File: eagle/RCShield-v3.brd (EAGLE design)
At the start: 92.7 x 82.5 mm, 52 parts, among them J1/J2 JOYSTICKPTH, P1/P3 POT, P2/P4 POT, Q1 MMBT3906, U1 TOUSCRUINO_SHIELD, U2 FT232RL-BASICSSOP, U4 XBEE, X1 USBSMD

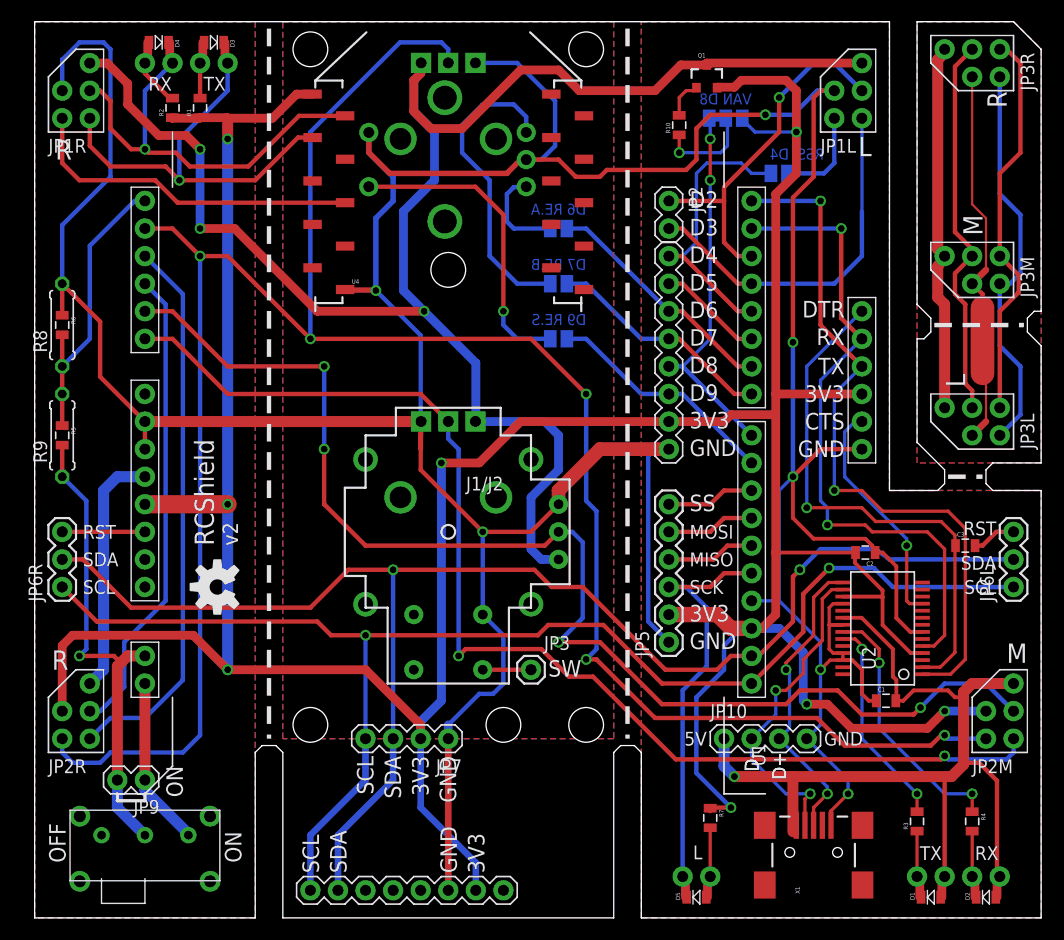
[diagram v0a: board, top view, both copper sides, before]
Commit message: 
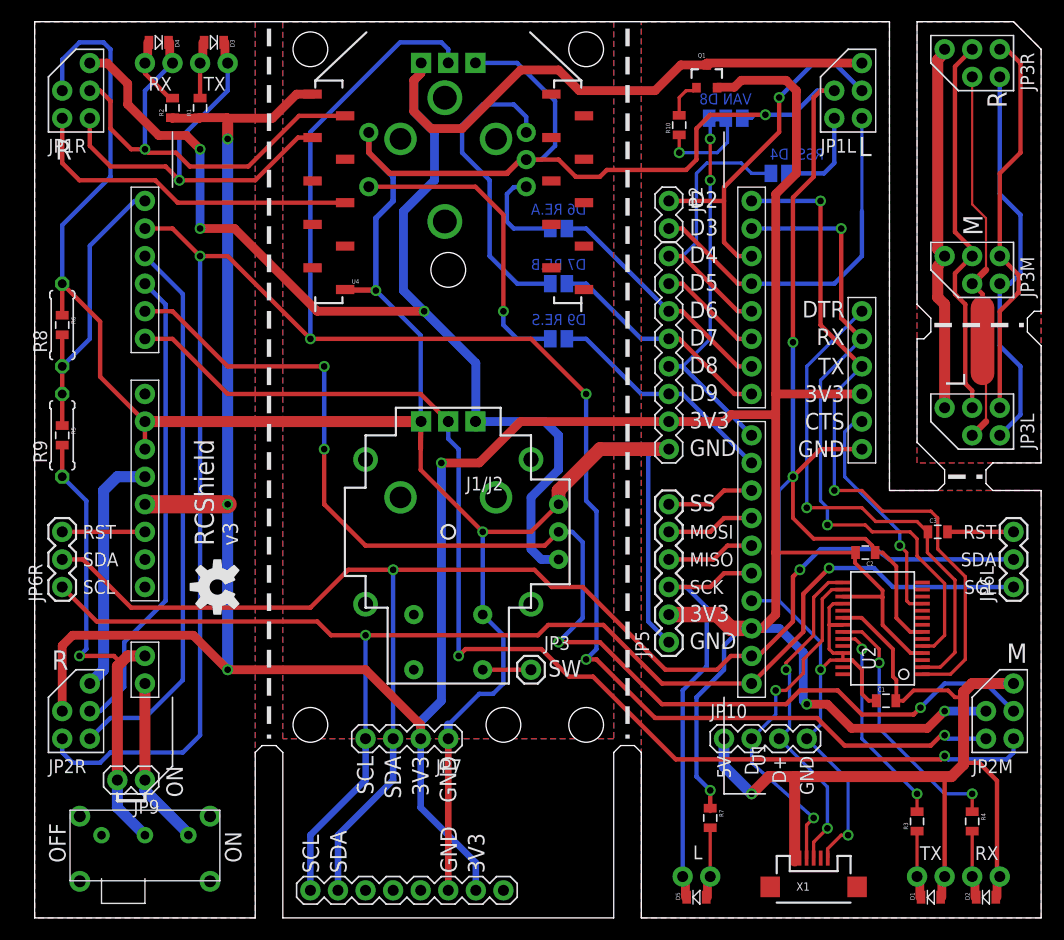
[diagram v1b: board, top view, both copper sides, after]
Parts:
- X1: value USBSMD -> USB-MICROB; device SparkFun:USB-MINIB -> SparkFun:USB-MICROB
- moved X1 3.17 mm to (71.8, 2.86), turned to 0 degrees
- moved C3 2.84 mm to (83.2, 35.6)
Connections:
- net 3.3V: no longer SJ2.3
- net GND: now also SJ2.3
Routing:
- net 3.3V: track 350.0 -> 341.5 mm, vias 8 -> 7
- net VUSB: track 84.0 -> 92.0 mm
- net GND: track 403.4 -> 409.2 mm
- net D+: track 28.2 -> 31.2 mm
- net D-: track 30.1 -> 32.2 mm
- net N$1: track 4.07 -> 6.09 mm
- net U_TX: track 65.8 -> 64.8 mm
- net U_RX: track 60.3 -> 59.4 mm
- net U_DTR: track 49.3 -> 48.6 mm
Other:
- board text added: "v3"
- board text removed: "v2"

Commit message: 
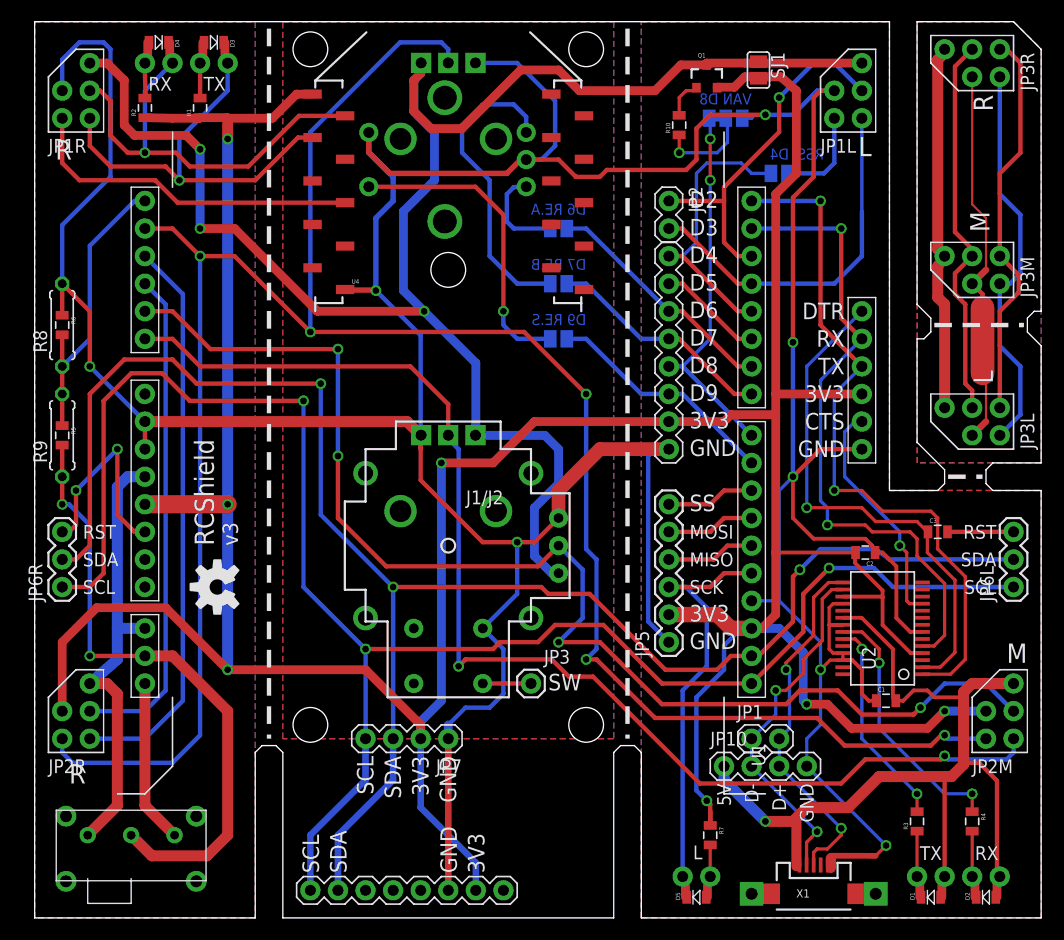
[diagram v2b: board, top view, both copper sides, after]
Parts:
- removed JP9: ON-OFF, wibauxl:1X02
- added JP1: USB, wibauxl:1X02
- added SJ1: (no value), wibauxl:SJ
- X1: value USB-MICROB -> USB; device SparkFun:USB-MICROB -> wibauxl:USB-MICROB
- moved JP10 2.54 mm to (63.5, 14.0)
- moved R2 2.54 mm to (10.2, 74.6)
- moved R7 1.59 mm to (62.2, 7.62)
- moved J1/J2 1.27 mm to (38.1, 34.3)
- moved JP3 1.27 mm to (45.7, 21.6)
- moved S4 1.27 mm to (8.89, 7.62)
- moved P1/P3 1.27 mm to (38.1, 37.5)
- moved X1 0.63 mm to (71.8, 2.22)
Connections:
- net 3.3V: now also SJ1.2
- net D+: now also JP1.2
- net D-: now also JP1.1
- net V+: no longer JP9.2
- net VAN: now also SJ1.1
- net VBAT: no longer JP9.1
- net _VUSB: now also S4.1, U1.5V@0, U1.5V@1; no longer U1.5V
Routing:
- net SCL: track 124.9 -> 160.3 mm, vias 2 -> 3
- net SDA: track 133.7 -> 159.7 mm, vias 2 -> 3
- net _VUSB: track 22.6 -> 41.8 mm
- net V+: track 44.2 -> 57.5 mm, vias 1 -> 2
- net RES: track 7.62 -> 19.3 mm, vias 0 -> 2
- net 3.3V: track 341.5 -> 352.2 mm
- net GND: track 409.2 -> 416.7 mm, vias 7 -> 8
- net VAN: track 158.6 -> 165.5 mm
- net A0: track 110.5 -> 113.8 mm
- net A2: track 43.6 -> 46.0 mm
- net D+: track 31.2 -> 33.5 mm
- net N$8: track 4.50 -> 2.91 mm
- net N$25: track 4.43 -> 3.23 mm
- net A3: track 51.3 -> 52.4 mm
- net A1: track 115.7 -> 116.4 mm
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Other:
- board text removed: "OFF"
- board text removed: "ON"

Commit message: 
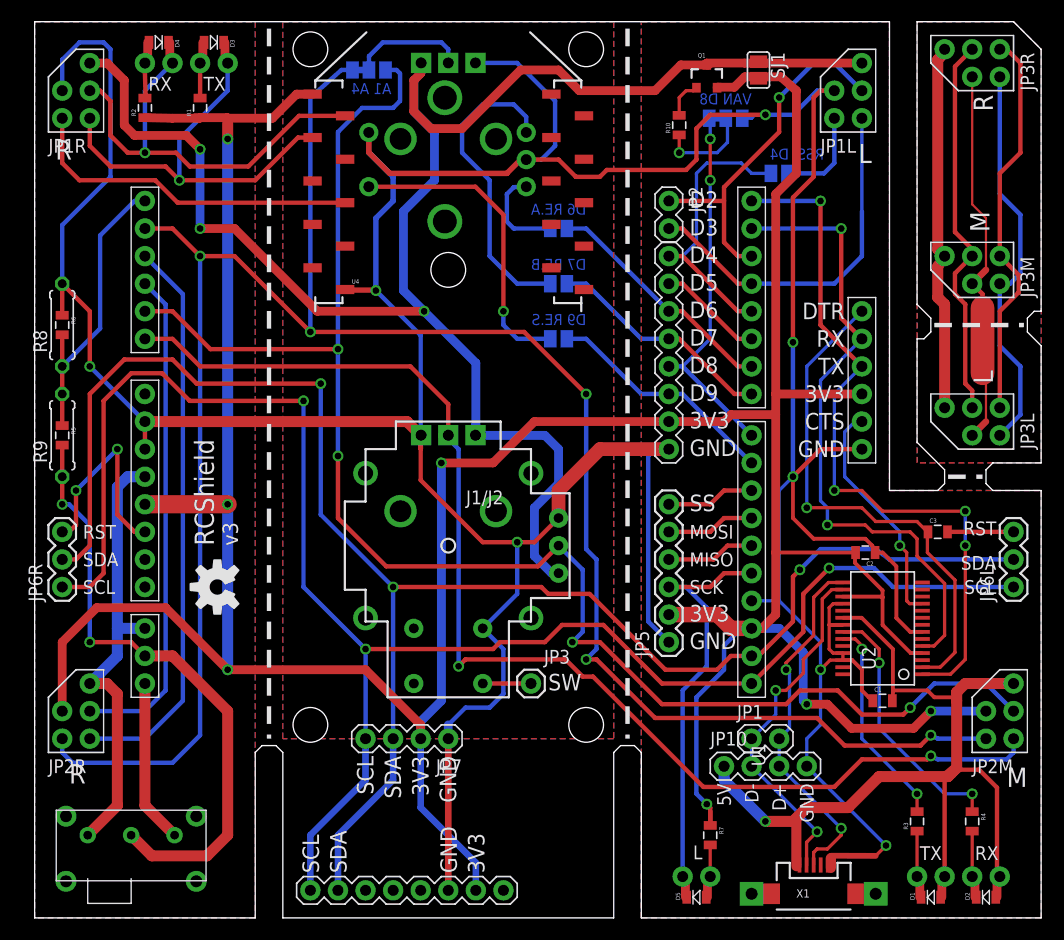
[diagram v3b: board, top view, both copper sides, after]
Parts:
- added SJ7: (no value), wibauxl:SJ_2WAYS_1-2
- JP10: value (none) -> USB
- JP4, JP7: value (none) -> I2C
- moved C1 0.32 mm to (78.1, 20.0)
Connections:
- new net N$7: P2/P4.P$2, SJ7.2
- net A1: now also SJ7.3
- net A4: now also SJ7.1; no longer P2/P4.P$2
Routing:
- net A1: track 116.4 -> 145.5 mm
- net N$7: track 0.00 -> 10.6 mm
- net A4: track 208.4 -> 198.8 mm
- net U_TX: track 64.8 -> 66.7 mm, vias 2 -> 4
- net VUSB: track 91.4 -> 93.0 mm
- net V+: track 57.5 -> 56.8 mm
- net GND: track 416.7 -> 416.2 mm
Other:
- board text added: "A1 A4"
